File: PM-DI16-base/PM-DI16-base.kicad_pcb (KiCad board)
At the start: 4 copper layers, 99.1 x 99.1 mm, 70 parts, among them J1 Conn_02x08_socket, J10 2EDGR-5.08-02P, J11 2EDGR-5.08-02P, J12 Conn_01x03, J13 Conn_01x03, J14 Conn_01x03, J16 S4B-PH-SM4-TB, J18 S4B-PH-SM4-TB, J19 Conn_02x08_socket, J3 2EDGR-5.08-02P, J4 2EDGR-5.08-02P, J5 2EDGR-5.08-02P, J6 2EDGR-5.08-02P, J7 2EDGR-5.08-02P, J8 2EDGR-5.08-02P, J9 2EDGR-5.08-02P, U1 PC817, U10 PC817, U11 PC817, U12 PC817, U13 PC817, U14 PC817, U15 PC817, U16 PC817, U17 PCA9555PW, U18 64900001039, U2 PC817, U3 PC817, U4 PC817, U5 PC817, U6 PC817, U7 PC817, U8 PC817, U9 PC817

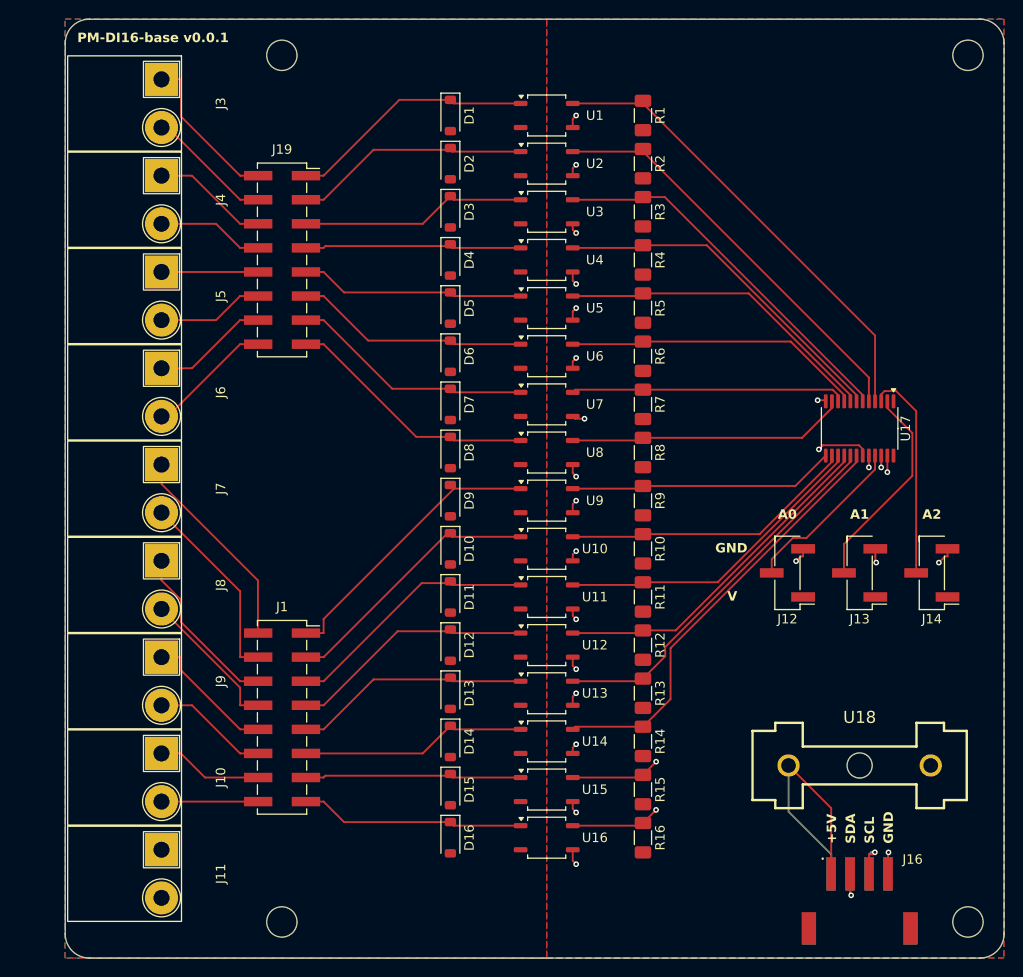
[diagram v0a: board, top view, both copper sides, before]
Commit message: fix PC817 footprint
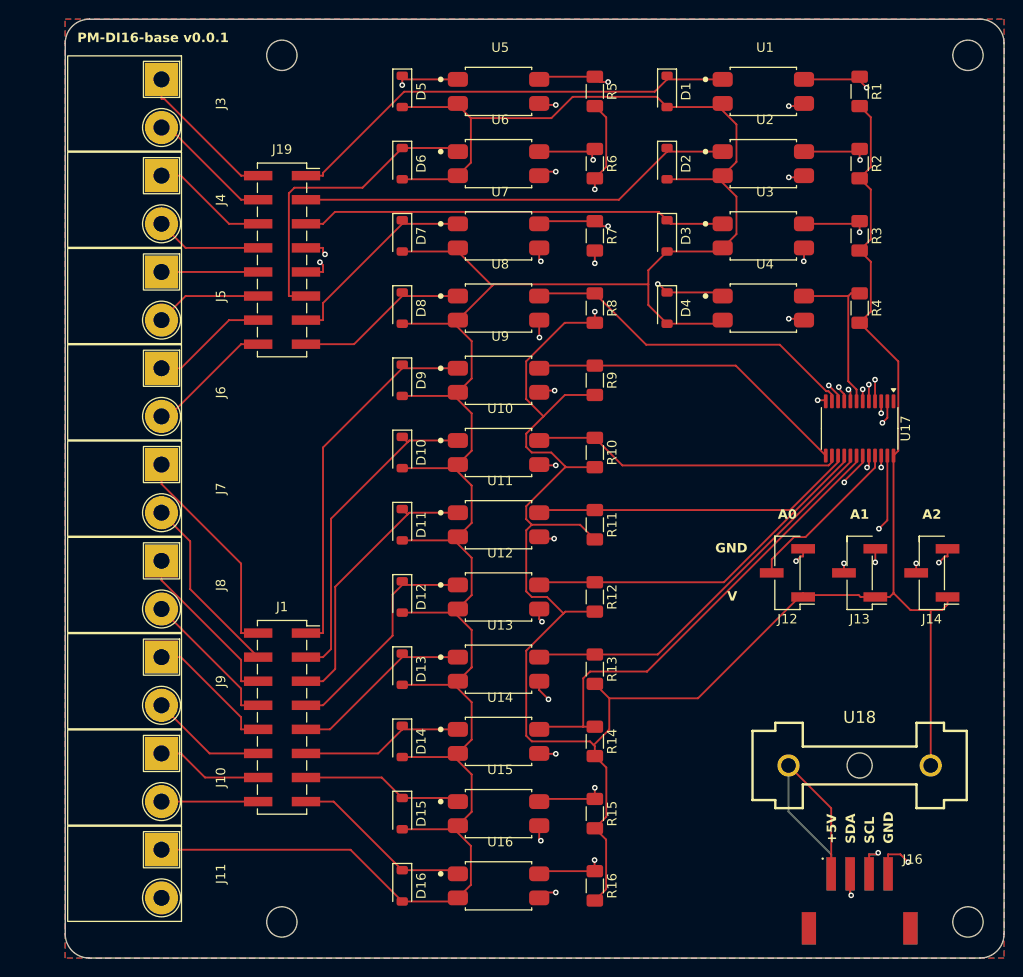
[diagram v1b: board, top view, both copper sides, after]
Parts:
- U1, U10, U11, U12, U13, U14, U15, U16, U2, U3, U4, U5, U6, U7, U8, U9: footprint Package_SO:SOP-4_3.8x4.1mm_P2.54mm -> NextPCB:PC817XI_SOIC254P975X460-4N
- moved D5 23.4 mm to (137.2, 58.4)
- moved R5 23.4 mm to (157.5, 58.4)
- moved U5 23.4 mm to (147.3, 58.4)
- moved D4 23.4 mm to (165.1, 81.3)
- moved R4 23.4 mm to (185.4, 81.3)
- moved U4 23.4 mm to (175.3, 81.3)
- moved D1 23.0 mm to (165.1, 58.4)
- moved D3 23.0 mm to (165.1, 73.7)
- moved R1 23.0 mm to (185.4, 58.4)
- moved R3 23.0 mm to (185.4, 73.7)
- moved U1 23.0 mm to (175.3, 58.4)
- moved U3 23.0 mm to (175.3, 73.7)
- moved D2 22.9 mm to (165.1, 66.0)
- moved R2 22.9 mm to (185.4, 66.0)
- moved U2 22.9 mm to (175.3, 66.0)
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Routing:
- net /M: track 0.00 -> 277.1 mm
- net VDD: track 0.00 -> 253.7 mm, vias 0 -> 3
- net Net-(D4-K): track 23.0 -> 46.3 mm, vias 0 -> 2
- net Net-(D1-K): track 26.1 -> 48.7 mm
- net Net-(D2-K): track 25.1 -> 46.5 mm
- net Net-(D3-K): track 24.0 -> 45.0 mm
- net Net-(U17-IO0_3): track 37.3 -> 17.5 mm
- net Net-(U17-IO0_4): track 34.5 -> 51.9 mm, vias 0 -> 2
- net Net-(U17-IO0_2): track 40.0 -> 25.0 mm, vias 0 -> 2
- net Net-(U17-IO0_5): track 31.8 -> 44.5 mm, vias 0 -> 2
- net Net-(U17-IO0_1): track 43.9 -> 32.9 mm, vias 0 -> 2
- net Net-(U17-IO0_6): track 29.0 -> 39.9 mm, vias 0 -> 2
- net Net-(D9-K): track 30.4 -> 39.5 mm
- net GND: track 29.8 -> 38.5 mm
- net Net-(U17-IO0_0): track 49.3 -> 40.8 mm, vias 0 -> 2
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- added copper zone on F.Cu, net (none)
- removed copper zone on F.Cu, net /M
- removed copper zone on F.Cu, net VDD

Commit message: Update PM-DI16-base.kicad_pcb
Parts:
- moved J19 15.9 mm to (116.8, 90.2)
- moved J1 14.8 mm to (116.8, 111.8)
- moved H1 12.7 mm to (137.2, 54.6)
- moved H4 12.7 mm to (137.2, 146.1)
- moved R1 11.4 mm to (195.6, 63.5)
- moved R2 11.4 mm to (195.6, 71.1)
- moved R3 11.4 mm to (195.6, 78.7)
- moved R4 11.4 mm to (195.6, 86.4)
- moved D1 11.4 mm to (175.3, 63.5)
- moved D2 11.4 mm to (175.3, 71.1)
- moved D3 11.4 mm to (175.3, 78.7)
- moved D4 11.4 mm to (175.3, 86.4)
- moved U1 11.4 mm to (185.4, 63.5)
- moved U2 11.4 mm to (185.4, 71.1)
- moved U3 11.4 mm to (185.4, 78.7)
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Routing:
- net /M: track 277.1 -> 0.00 mm
- net VDD: track 253.7 -> 0.00 mm, vias 3 -> 0
- net Net-(U17-IO1_7): track 61.8 -> 0.00 mm, vias 2 -> 0
- net Net-(U17-IO1_6): track 53.9 -> 0.00 mm, vias 2 -> 0
- net /SDA: track 52.8 -> 0.00 mm, vias 2 -> 0
- net Net-(U17-IO0_4): track 51.9 -> 0.00 mm, vias 2 -> 0
- net Net-(U17-IO1_5): track 50.1 -> 0.00 mm
- net Net-(D1-K): track 48.7 -> 0.00 mm
- net /SCL: track 48.5 -> 0.00 mm, vias 2 -> 0
- net Net-(D2-K): track 46.5 -> 0.00 mm
- net Net-(D4-K): track 46.3 -> 0.00 mm, vias 2 -> 0
- net Net-(D3-K): track 45.0 -> 0.00 mm
- net Net-(U17-IO0_5): track 44.5 -> 0.00 mm, vias 2 -> 0
- net Net-(U17-IO1_4): track 42.0 -> 0.00 mm
- net Net-(U17-IO0_0): track 40.8 -> 0.00 mm, vias 2 -> 0
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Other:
- copper layers 4 -> 2
- board text added: "PM-DI16-base v0.0.2"
- board text removed: "PM-DI16-base v0.0.1"

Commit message: v0.0.2
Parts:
- removed J1, J19: Conn_02x08_socket, Connector_PinSocket_2.54mm:PinSocket_2x08_P2.54mm_Vertical_SMD
- removed J3, J4, J5, J6, J7, J8, J9: 2EDGR-5.08-02P, NextPCB:Degson_2EDGR-5.08-02P
- added logo_kicad: KiCad-Logo2_8mm_SilkScreen, Symbol:KiCad-Logo2_8mm_SilkScreen, B.Cu at (180.3, 58.4)
- added logo_oshw: OSHW-Symbol_13.4x12mm_SilkScreen, Symbol:OSHW-Symbol_13.4x12mm_SilkScreen, B.Cu at (180.3, 73.7)
- J10: value 2EDGR-5.08-02P -> 2EDGR-5.08-18P; footprint NextPCB:Degson_2EDGR-5.08-02P -> NextPCB:Degson_2EDGR-5.08-18P
- J11: value 2EDGR-5.08-02P -> Conn_02x16_socket; footprint NextPCB:Degson_2EDGR-5.08-02P -> NextPCB:Conn_02x16_socket
- J15: renamed from J18; moved to F.Cu
- moved J10 71.1 mm to (106.7, 57.1)
- moved R1 62.2 mm to (133.3, 62.2), turned to 0 degrees
- moved R2 54.1 mm to (142.2, 62.2), turned to 0 degrees
- moved U1 52.8 mm to (133.3, 72.4), turned to 90 degrees
- moved D8 50.8 mm to (195.6, 82.5), turned to 0 degrees
- moved R3 47.4 mm to (151.1, 62.2), turned to 0 degrees
- moved D1 46.0 mm to (133.3, 82.5), turned to 0 degrees
- moved U2 43.2 mm to (142.2, 72.4), turned to 90 degrees
- moved R4 43.0 mm to (160.0, 62.2), turned to 0 degrees
- moved D7 42.8 mm to (186.7, 82.5), turned to 0 degrees
- moved U8 41.6 mm to (195.6, 72.4), turned to 90 degrees
- moved J11 39.4 mm to (116.8, 100.3), turned to 0 degrees
- moved D6 36.9 mm to (177.8, 82.5), turned to 0 degrees
- moved R8 35.9 mm to (195.6, 62.2), turned to 0 degrees
- moved D2 34.9 mm to (142.2, 82.5), turned to 0 degrees
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- renumbered J16 to J13, J12 to J16, J13 to J17, J14 to J18
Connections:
- J10 pad 1: Net-(J1-Pin_14) -> Net-(J10-Pin_1)
- J10 pad 2: Net-(J1-Pin_16) -> Net-(J10-Pin_2)
- J11 pad 1: /M -> Net-(D1-K)
- J11 pad 2: unconnected-(J11-Pin_2-Pad2) -> Net-(J10-Pin_1)
- J13 pad 1: Net-(J16-Pad1) -> Net-(J13-Pad1)
- J15 pad 1: GND -> Net-(J13-Pad1)
- J15 pad 2: /SCL -> /SDA
- J15 pad 3: /SDA -> /SCL
- J15 pad 4: Net-(J16-Pad1) -> GND
- U18 pad 2: Net-(J16-Pad1) -> Net-(J13-Pad1)
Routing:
- net /M: track 0.00 -> 334.4 mm, vias 0 -> 2
- net VDD: track 0.00 -> 313.4 mm, vias 0 -> 1
- net Net-(D8-K): track 0.00 -> 87.5 mm
- net Net-(D7-K): track 0.00 -> 77.5 mm
- net Net-(U17-IO0_0): track 0.00 -> 76.0 mm, vias 0 -> 2
- net Net-(D12-K): track 0.00 -> 74.1 mm
- net Net-(D6-K): track 0.00 -> 67.6 mm
- net Net-(U17-IO1_4): track 0.00 -> 65.6 mm
- net Net-(U17-IO0_1): track 0.00 -> 64.8 mm, vias 0 -> 2
- net /SCL: track 0.00 -> 60.7 mm, vias 0 -> 2
- net Net-(U17-IO1_0): track 0.00 -> 58.2 mm
- net Net-(D5-K): track 0.00 -> 57.8 mm
- net Net-(U17-IO1_5): track 0.00 -> 57.4 mm
- net /SDA: track 0.00 -> 57.3 mm
- net Net-(U17-IO0_2): track 0.00 -> 57.1 mm, vias 0 -> 2
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
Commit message: send to nextpcb
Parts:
- R1, R10, R11, R12, R13, R14, R15, R16, R2, R3, R4, R5, R6, R7, R8, R9: footprint Resistor_SMD:R_1206_3216Metric_Pad1.30x1.75mm_HandSolder -> Resistor_SMD:R_1206_3216Metric
